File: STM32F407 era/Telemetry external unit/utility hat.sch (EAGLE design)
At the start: 4 parts, among them U1 SC18IM700IPW,112, U2 MAX1704X

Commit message: Initial Rasp Pi UPS design done
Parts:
- added C1, C2: 10u, microbuilder:CAP_CERAMIC_0805MP
- added C3: 1,8n, microbuilder:CAP_CERAMIC_0603MP
- added C4: 47p, microbuilder:CAP_CERAMIC_0603MP
- added C5, C6: 100u, microbuilder:CAP_CERAMIC1206
- added CN1: (no value), microbuilder:JST_4PIN
- added CN2: (no value), adafruit:USBMINIB
- added D1: B320A-13-F, diode:MBRS320T3
- added J1: (no value), SparkFun-Connectors:JST_2MM_MALE
- added L1: (no value), microbuilder:INDUCTOR
- added R1, R2, R3: 150, microbuilder:RESISTOR_0603MP
- added R10: 17k4, microbuilder:RESISTOR_0603MP
- added R4, R5: 1k, microbuilder:RESISTOR_0603MP
- added R6: 150k, microbuilder:RESISTOR_0603MP
- added R7: 1M, microbuilder:RESISTOR_0603MP
- added R8: 11k 1%, microbuilder:RESISTOR_0603MP
- added R9: 34k8 1%, microbuilder:RESISTOR_0603MP
- added U$10: APC220, APC220:APC220
- added U3: LTC3872ETS8TRMPBF, LTC_By_element14_Batch_1:LTC3872ETS8TRMPBF
- added U4: MCP73833-AMI/UN, Microchip_By_element14_Batch_1:MCP73833-AMI/UN
- added U5: Si3460DDV, Vishay_By_element14_Batch_1:SI3457CDV-T1-GE3
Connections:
- new net N$1: U$10.RXD, U1.TX
- new net N$10: C1.P$1, J1.+, L1.1, R7.2, U2.CELL, U3.IPRG, U3.VIN, U4.VBAT, U4.VBAT_2
- new net N$11: R4.2, U4.PROG
- new net N$12: R5.1, U4.THERM
- new net N$13: R5.2, R6.2
- new net N$14: R7.1, U3.RUN/SS
- new net N$15: R8.2, R9.2, U3.VFB
- new net N$16: C4.P$1, R10.2, U3.ITH
- new net N$17: C3.P$1, R10.1
- new net N$19: D1.A, L1.2, U3.SW, U5.D, U5.D_2, U5.D_3, U5.D_4
- new net N$2: U$10.TXD, U1.RX
- new net N$21: U3.NGATE, U5.G
- new net N$3: C2.P$1, CN1.4, CN2.VBUS, U4.VDD, U4.VDD_2
- new net N$4: R1.2, U4.STAT1
- new net N$5: R2.2, U4.STAT2
- new net N$6: R3.2, U4.*PG
- new net N$7: CN1.1, R3.1
- new net N$8: CN1.2, R2.1
- new net N$9: CN1.3, R1.1
- net 3.3V: now also U$10.VCC
- net 5.0V: now also C5.P$1, C6.P$1, D1.C, R9.1
- net GND: now also C1.P$2, C2.P$2, C3.P$2, C4.P$2, C5.P$2, C6.P$2, CN2.GND, J1.-, R4.1, R6.1, R8.1, U$10.GND, U3.GND, U4.VSS, U5.S
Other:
- moved on the sheet: JP1, U1, U2

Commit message: minor changes
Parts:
- added BAT1, BAT2, BAT3, BAT4, BAT5, BAT6: (no value), SparkFun-Electromechanical:BATTERY18650
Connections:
- new net N$18: BAT1.-, BAT2.-, BAT3.-, BAT4.-, BAT5.-, BAT6.-
- new net N$20: BAT1.+, BAT2.+, BAT3.+, BAT4.+, BAT5.+, BAT6.+
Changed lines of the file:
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@@
 <part name="U5" library="Vishay_By_element14_Batch_1" deviceset="SI3457CDV-T1-GE3" device="" value="Si3460DDV"/>
 <part name="U$28" library="microbuilder" deviceset="GND" device=""/>
+<part name="BAT1" library="SparkFun-Electromechanical" deviceset="BATTERY" device="18650"/>
+<part name="BAT2" library="SparkFun-Electromechanical" deviceset="BATTERY" device="18650"/>
+<part name="BAT3" library="SparkFun-Electromechanical" deviceset="BATTERY" device="18650"/>
+<part name="BAT4" library="SparkFun-Electromechanical" deviceset="BATTERY" device="18650"/>
+<part name="BAT5" library="SparkFun-Electromechanical" deviceset="BATTERY" device="18650"/>
+<part name="BAT6" library="SparkFun-Electromechanical" deviceset="BATTERY" device="18650"/>
 </parts>
 <sheets>
@@
 <instance part="U5" gate="A" x="129.54" y="0"/>
 <instance part="U$28" gate="G$1" x="109.22" y="-7.62"/>
+<instance part="BAT1" gate="G$1" x="-30.48" y="-58.42" rot="R270"/>
+<instance part="BAT2" gate="G$1" x="-15.24" y="-58.42" rot="R270"/>
+<instance part="BAT3" gate="G$1" x="0" y="-58.42" rot="R270"/>
+<instance part="BAT4" gate="G$1" x="15.24" y="-58.42" rot="R270"/>
+<instance part="BAT5" gate="G$1" x="30.48" y="-58.42" rot="R270"/>
+<instance part="BAT6" gate="G$1" x="45.72" y="-58.42" rot="R270"/>
 </instances>
 <busses>
@@
 </segment>
 </net>
+<net name="N$18" class="0">
+<segment>
+<pinref part="BAT1" gate="G$1" pin="-"/>
+<wire x1="-30.48" y1="-63.5" x2="-30.48" y2="-66.04" width="0.1524" layer="91"/>
+<pinref part="BAT2" gate="G$1" pin="-"/>
+<wire x1="-30.48" y1="-66.04" x2="-15.24" y2="-66.04" width="0.1524" layer="91"/>
+<wire x1="-15.24" y1="-66.04" x2="-15.24" y2="-63.5" width="0.1524" layer="91"/>
+<pinref part="BAT3" gate="G$1" pin="-"/>
+<wire x1="-15.24" y1="-66.04" x2="0" y2="-66.04" width="0.1524" layer="91"/>
+<wire x1="0" y1="-66.04" x2="0" y2="-63.5" width="0.1524" layer="91"/>
+<junction x="-15.24" y="-66.04"/>
+<pinref part="BAT4" gate="G$1" pin="-"/>
+<wire x1="0" y1="-66.04" x2="15.24" y2="-66.04" width="0.1524" layer="91"/>
+<wire x1="15.24" y1="-66.04" x2="15.24" y2="-63.5" width="0.1524" layer="91"/>
+<junction x="0" y="-66.04"/>
+<pinref part="BAT5" gate="G$1" pin="-"/>
+<wire x1="15.24" y1="-66.04" x2="30.48" y2="-66.04" width="0.1524" layer="91"/>
+<wire x1="30.48" y1="-66.04" x2="30.48" y2="-63.5" width="0.1524" layer="91"/>
+<junction x="15.24" y="-66.04"/>
+<pinref part="BAT6" gate="G$1" pin="-"/>
+<wire x1="30.48" y1="-66.04" x2="45.72" y2="-66.04" width="0.1524" layer="91"/>
+<wire x1="45.72" y1="-66.04" x2="45.72" y2="-63.5" width="0.1524" layer="91"/>
+<junction x="30.48" y="-66.04"/>
+</segment>
+</net>
+<net name="N$20" class="0">
+<segment>
+<pinref part="BAT6" gate="G$1" pin="+"/>
+<wire x1="45.72" y1="-53.34" x2="45.72" y2="-50.8" width="0.1524" layer="91"/>
+<pinref part="BAT5" gate="G$1" pin="+"/>
+<wire x1="45.72" y1="-50.8" x2="30.48" y2="-50.8" width="0.1524" layer="91"/>
+<wire x1="30.48" y1="-50.8" x2="30.48" y2="-53.34" width="0.1524" layer="91"/>
+<pinref part="BAT4" gate="G$1" pin="+"/>
+<wire x1="30.48" y1="-50.8" x2="15.24" y2="-50.8" width="0.1524" layer="91"/>
+<wire x1="15.24" y1="-50.8" x2="15.24" y2="-53.34" width="0.1524" layer="91"/>
+<junction x="30.48" y="-50.8"/>
+<pinref part="BAT3" gate="G$1" pin="+"/>
+<wire x1="15.24" y1="-50.8" x2="0" y2="-50.8" width="0.1524" layer="91"/>
+<wire x1="0" y1="-50.8" x2="0" y2="-53.34" width="0.1524" layer="91"/>
+<junction x="15.24" y="-50.8"/>
+<pinref part="BAT2" gate="G$1" pin="+"/>
+<wire x1="0" y1="-50.8" x2="-15.24" y2="-50.8" width="0.1524" layer="91"/>
+<wire x1="-15.24" y1="-50.8" x2="-15.24" y2="-53.34" width="0.1524" layer="91"/>
+<junction x="0" y="-50.8"/>
+<pinref part="BAT1" gate="G$1" pin="+"/>
+<wire x1="-15.24" y1="-50.8" x2="-30.48" y2="-50.8" width="0.1524" layer="91"/>
+<wire x1="-30.48" y1="-50.8" x2="-30.48" y2="-53.34" width="0.1524" layer="91"/>
+<junction x="-15.24" y="-50.8"/>
+</segment>
+</net>

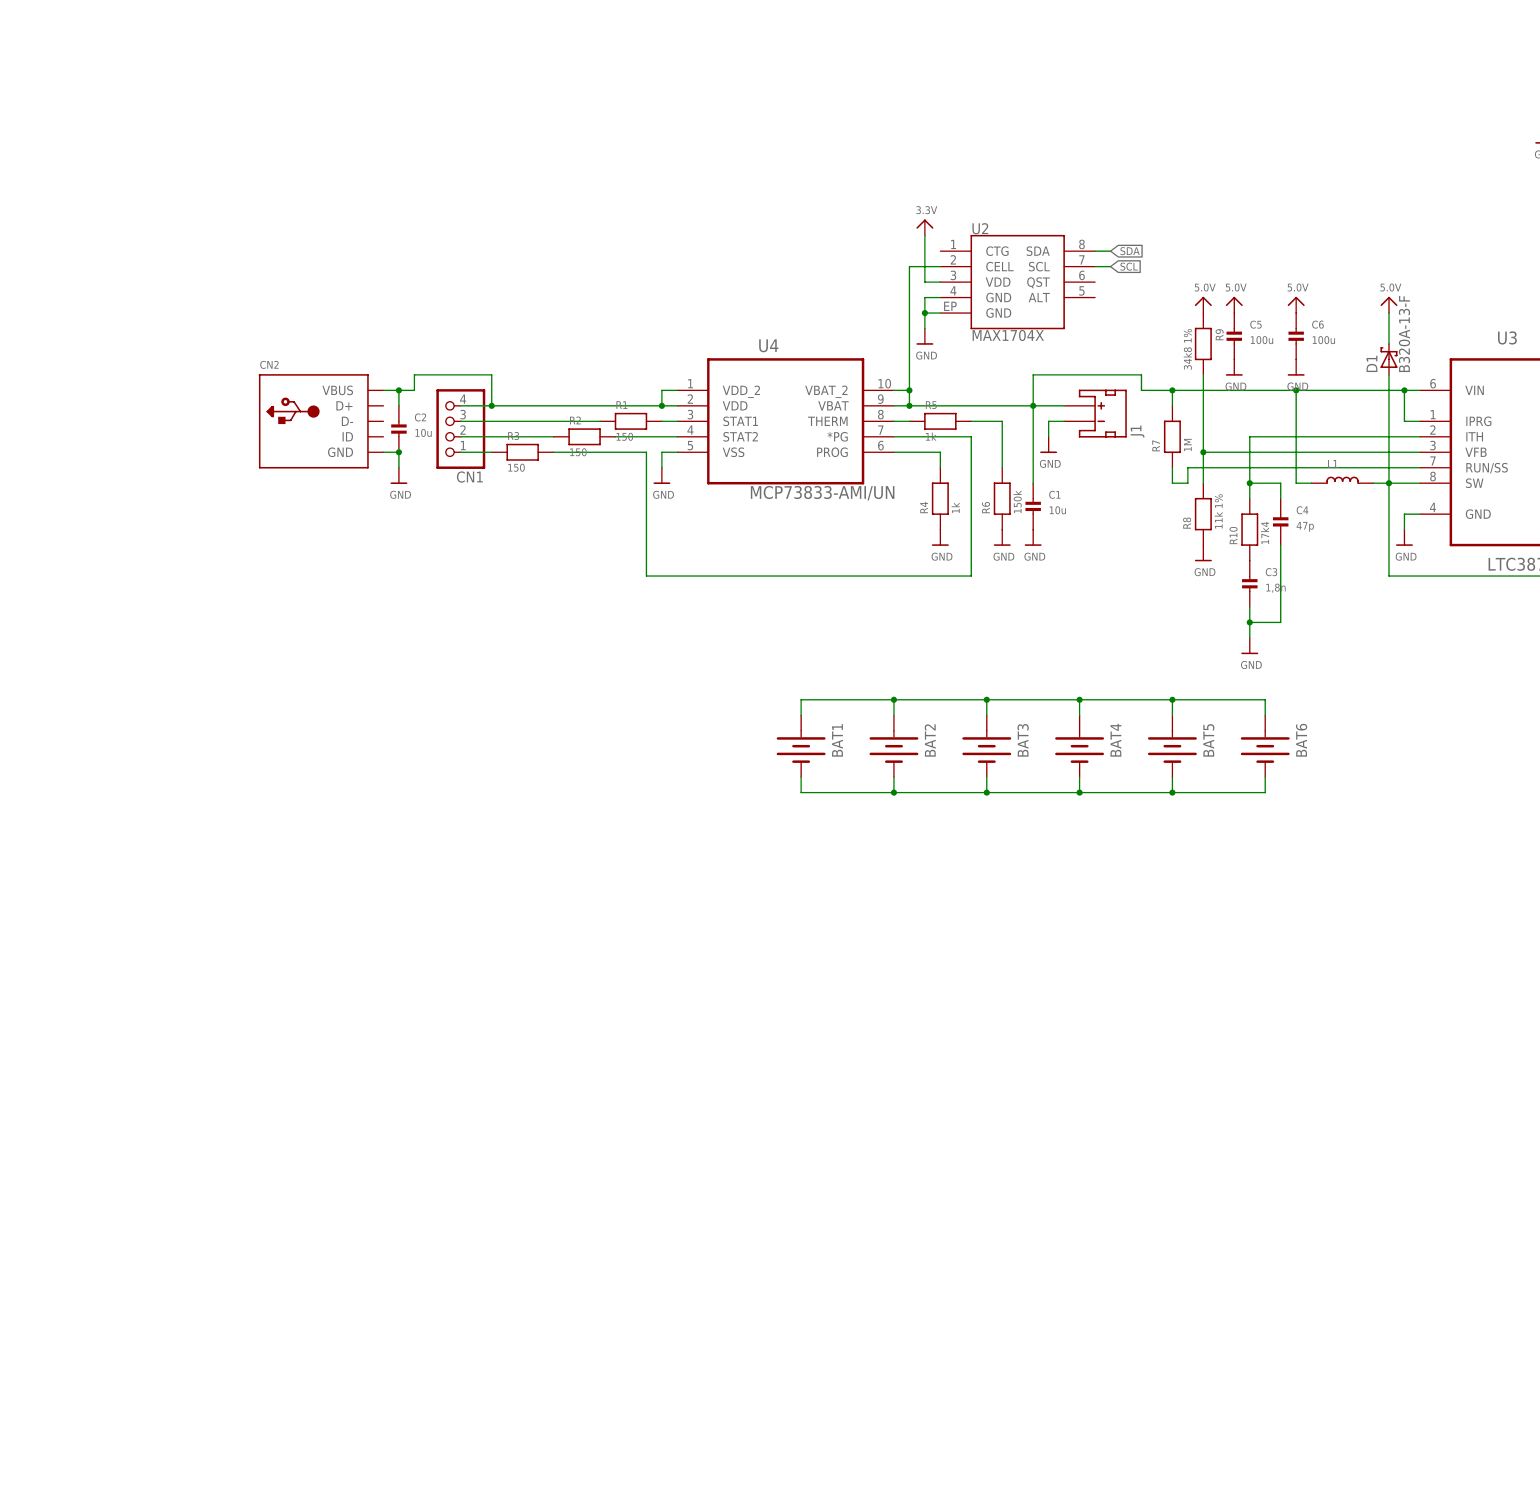
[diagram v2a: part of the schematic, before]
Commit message: changes to the charging circuit
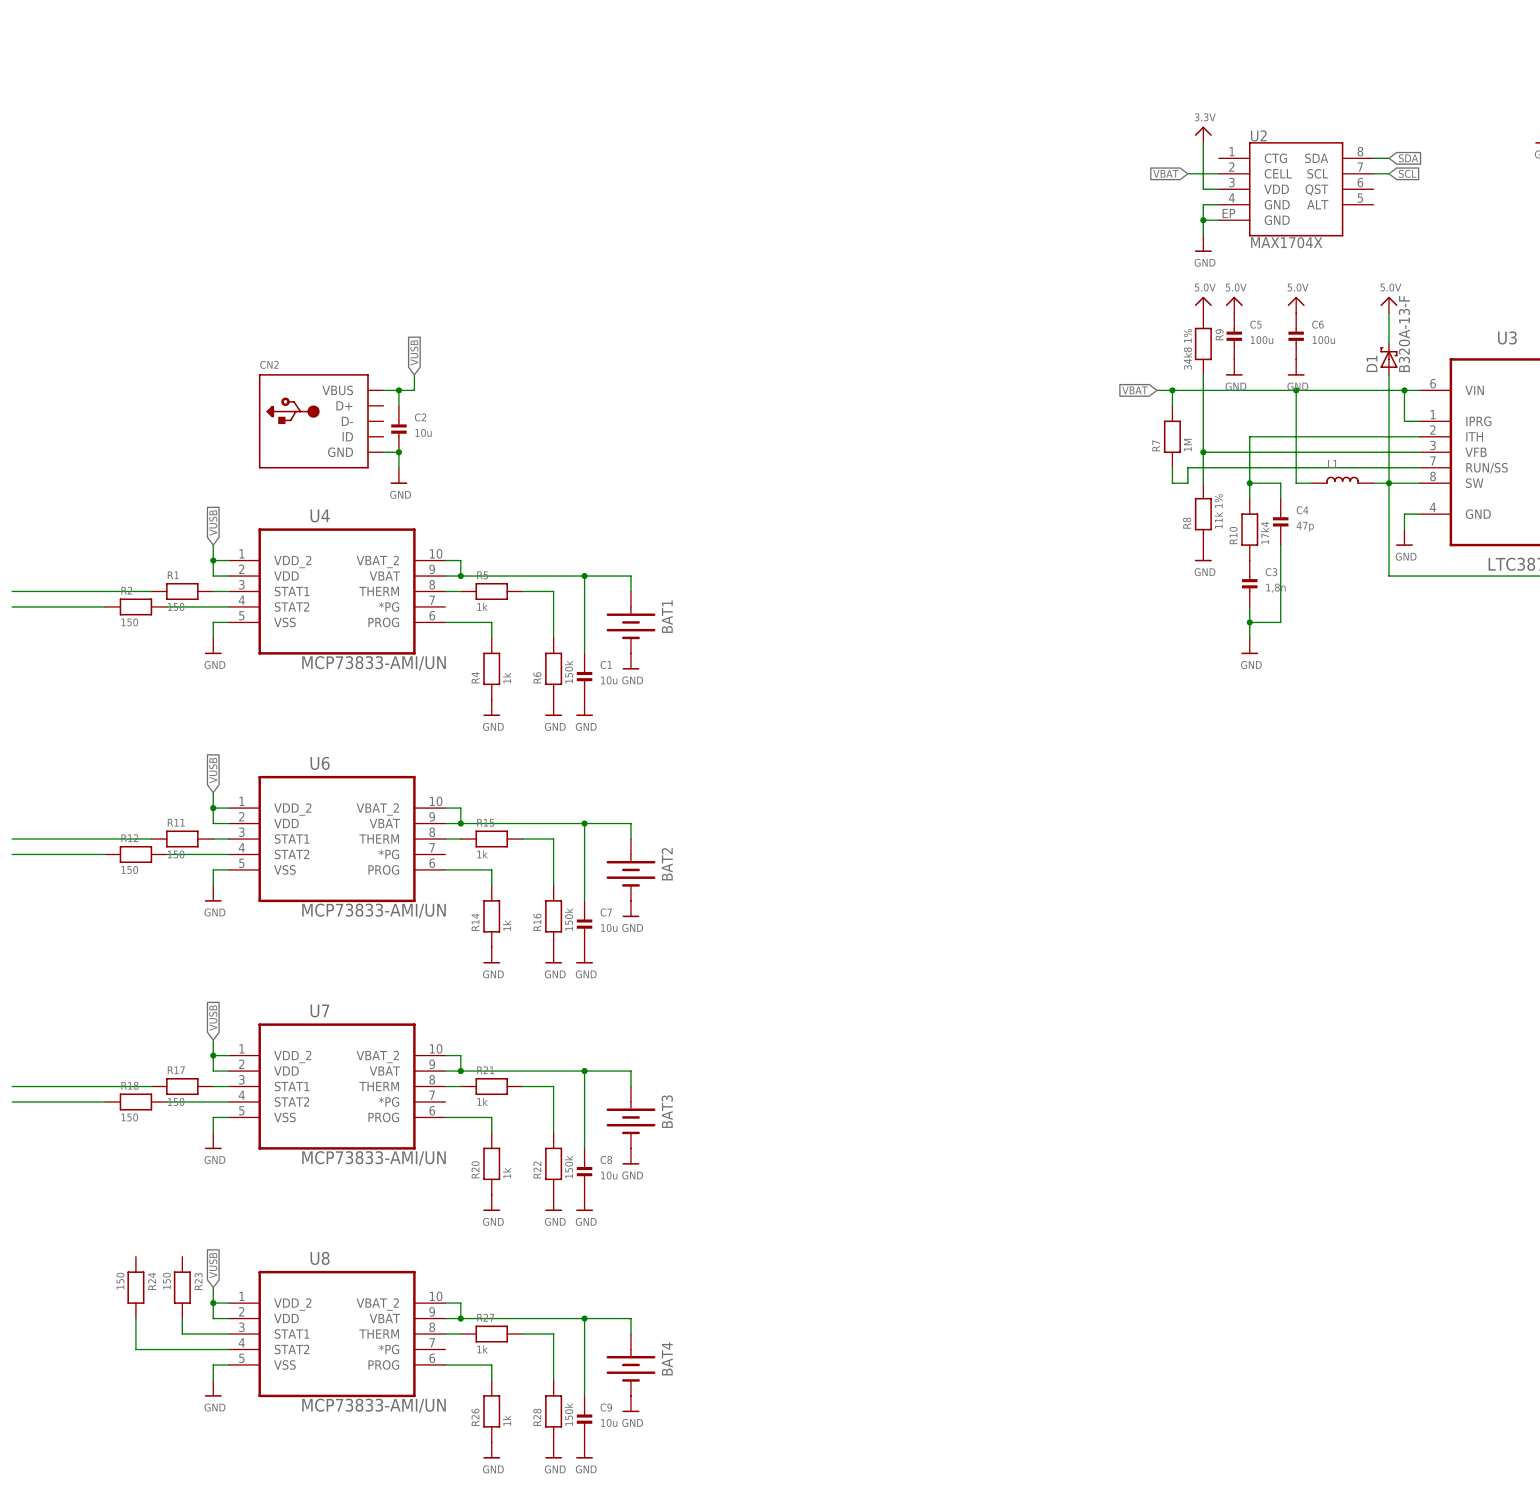
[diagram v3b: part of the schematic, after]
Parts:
- removed BAT5, BAT6: (no value), SparkFun-Electromechanical:BATTERY18650
- removed CN1: (no value), microbuilder:JST_4PIN
- removed J1: (no value), SparkFun-Connectors:JST_2MM_MALE
- removed R3: 150, microbuilder:RESISTOR_0603MP
- added C7, C8, C9: 10u, microbuilder:CAP_CERAMIC_0805MP
- added R11, R12, R17, R18, R23, R24: 150, microbuilder:RESISTOR_0603MP
- added R14, R15, R20, R21, R26, R27: 1k, microbuilder:RESISTOR_0603MP
- added R16, R22, R28: 150k, microbuilder:RESISTOR_0603MP
- added U6, U7, U8: MCP73833-AMI/UN, Microchip_By_element14_Batch_1:MCP73833-AMI/UN
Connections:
- removed net N$10: C1.P$1, J1.+, L1.1, R7.2, U2.CELL, U3.IPRG, U3.VIN, U4.VBAT, U4.VBAT_2
- removed net N$18: BAT1.-, BAT2.-, BAT3.-, BAT4.-, BAT5.-, BAT6.-
- removed net N$20: BAT1.+, BAT2.+, BAT3.+, BAT4.+, BAT5.+, BAT6.+
- removed net N$3: C2.P$1, CN1.4, CN2.VBUS, U4.VDD, U4.VDD_2
- removed net N$6: R3.2, U4.*PG
- removed net N$7: CN1.1, R3.1
- new net N$22: BAT1.+, C1.P$1, U4.VBAT, U4.VBAT_2
- new net N$26: R11.2, U6.STAT1
- new net N$27: R12.2, U6.STAT2
- new net N$30: R12.1
- new net N$31: R11.1
- new net N$32: R14.2, U6.PROG
- new net N$33: R15.1, U6.THERM
- new net N$34: R15.2, R16.2
- new net N$35: BAT2.+, C7.P$1, U6.VBAT, U6.VBAT_2
- new net N$37: R17.2, U7.STAT1
- new net N$38: R18.2, U7.STAT2
- new net N$41: R18.1
- new net N$42: R17.1
- new net N$43: R20.2, U7.PROG
- new net N$44: R21.1, U7.THERM
- new net N$45: R21.2, R22.2
- new net N$46: BAT3.+, C8.P$1, U7.VBAT, U7.VBAT_2
- new net N$48: R23.2, U8.STAT1
- new net N$49: R24.2, U8.STAT2
- new net N$54: R26.2, U8.PROG
- new net N$55: R27.1, U8.THERM
- new net N$56: R27.2, R28.2
- new net N$57: BAT4.+, C9.P$1, U8.VBAT, U8.VBAT_2
- new net VBAT: L1.1, R7.2, U2.CELL, U3.IPRG, U3.VIN
- new net VUSB: C2.P$1, CN2.VBUS, U4.VDD, U4.VDD_2, U6.VDD, U6.VDD_2, U7.VDD, U7.VDD_2, U8.VDD, U8.VDD_2
- net GND: now also BAT1.-, BAT2.-, BAT3.-, BAT4.-, C7.P$2, C8.P$2, C9.P$2, R14.1, R16.1, R20.1, R22.1, R26.1, R28.1, U6.VSS, U7.VSS, U8.VSS; no longer J1.-
- net N$8: no longer CN1.2
- net N$9: no longer CN1.3
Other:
- moved on the sheet: BAT1, BAT2, BAT3, BAT4, C1, R1, R2, R4, R5, R6, U2, U4
